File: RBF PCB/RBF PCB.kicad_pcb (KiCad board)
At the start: 2 copper layers, 40 x 70 mm, 10 parts, among them J1 DF11-12DP, J2 DF11-12DP, J5 DF11-12DP, J6 DF11-12DP, J9 B2B-XH-A

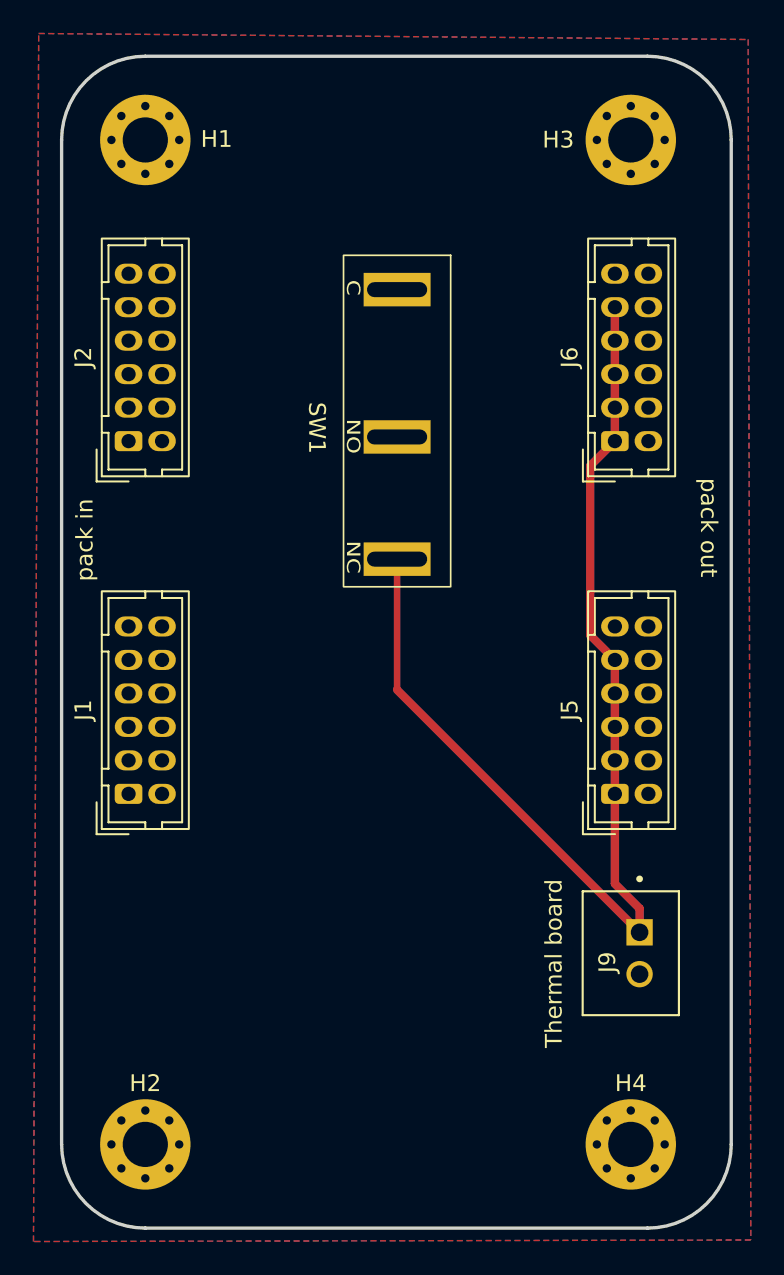
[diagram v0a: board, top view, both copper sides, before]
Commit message: updated mounting holes
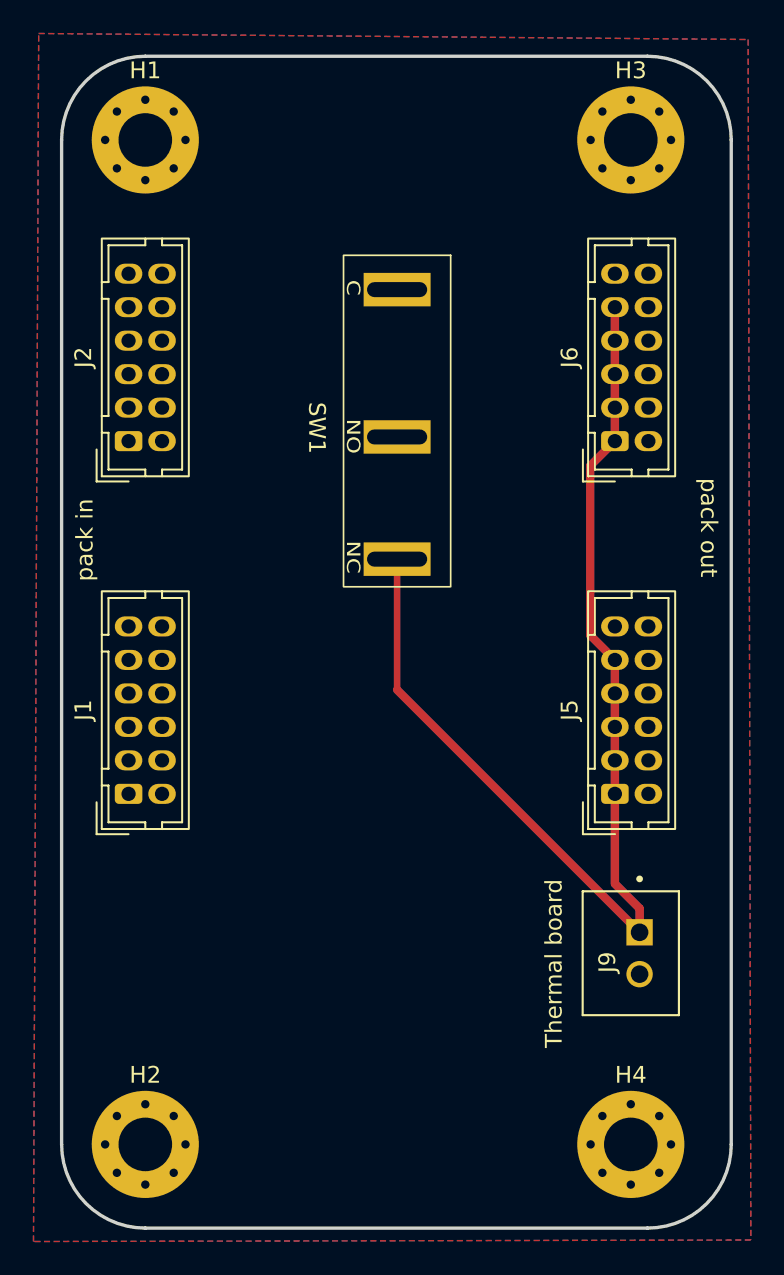
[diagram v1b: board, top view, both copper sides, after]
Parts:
- H1, H2, H3, H4: footprint MountingHole:MountingHole_2.7mm_M2.5_Pad_Via -> MountingHole:MountingHole_3.2mm_M3_Pad_Via

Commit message: .
.
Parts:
- H1, H2, H3, H4: footprint MountingHole:MountingHole_3.2mm_M3_Pad_Via -> MountingHole:MountingHole_2.7mm_M2.5_Pad_Via
